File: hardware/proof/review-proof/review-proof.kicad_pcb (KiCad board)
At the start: 4 copper layers, 92 x 60 mm, 26 parts, among them J1 MAINS, J2 5V_IN, J4 LOAD, U1 VO3526, U2 AMS1117-3.3, U3 MCP6001-OT, U4 ATtiny85-20M, Y1 8MHz

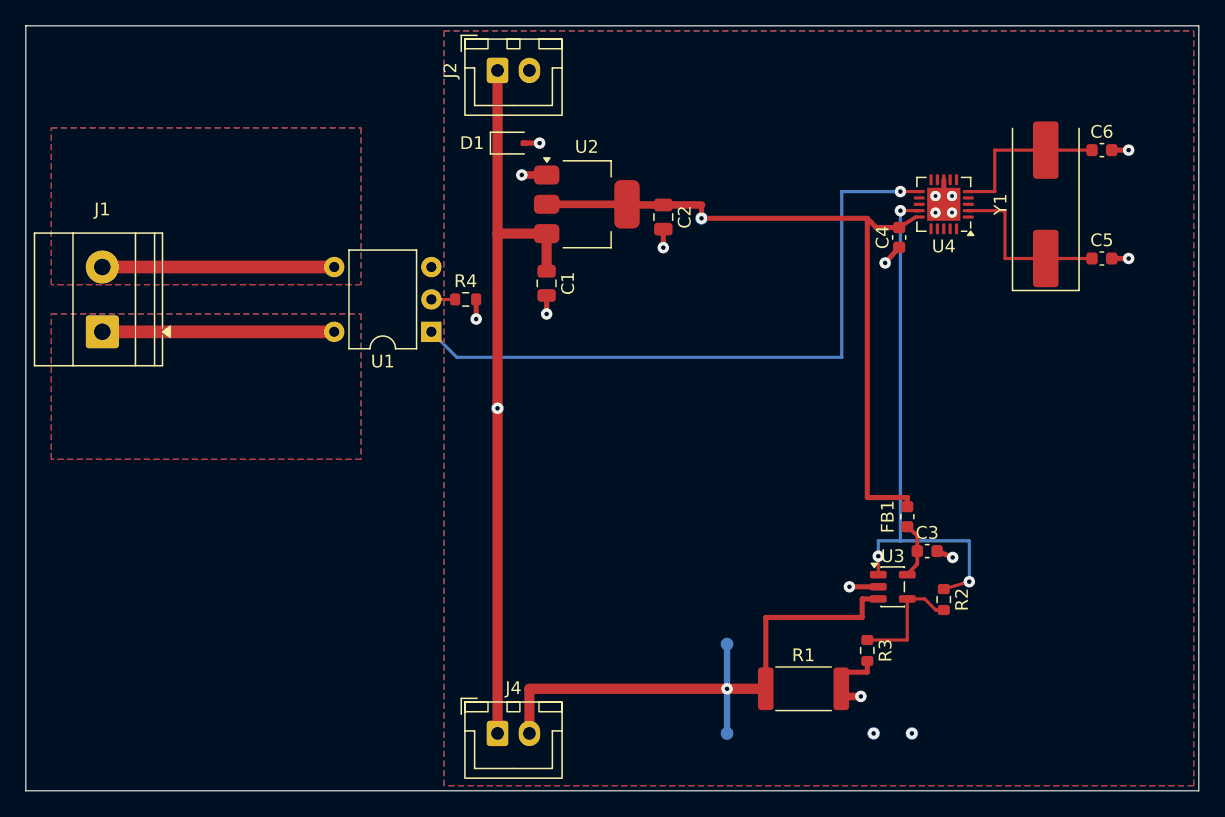
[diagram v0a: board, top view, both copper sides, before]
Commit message: feat(hardware): tidy the review proof design to the workmanship items [SOL-BOARD-LAYOUT-WORKMANSHIP-ITEMS.C3]
Redraw every route of the layout review proof design at 45 degrees, each
straight run at least 1 mm, each track at its class's width and entering
long pads along their axes, branching only at pads, and place R1, R2, R3,
FB1, C3, C4, C5, C6, J4 and the test points beside what they connect to,
so the board passes the pre-order check with every workmanship rule in
force. The tracks, parts and vias are changed through Konnect; the eleven
vias the tidy no longer needs, which Konnect cannot delete, are removed
with KiCad's own scripting API on the closed board. Give the Supply class
a 0.3 mm track width, set the measured rules' figures and the corner and
jog rules, and bring the floorplan, plan and rules table to the board.

Co-Authored-By: Claude Opus 5.5 (1M context) <noreply@anthropic.com>
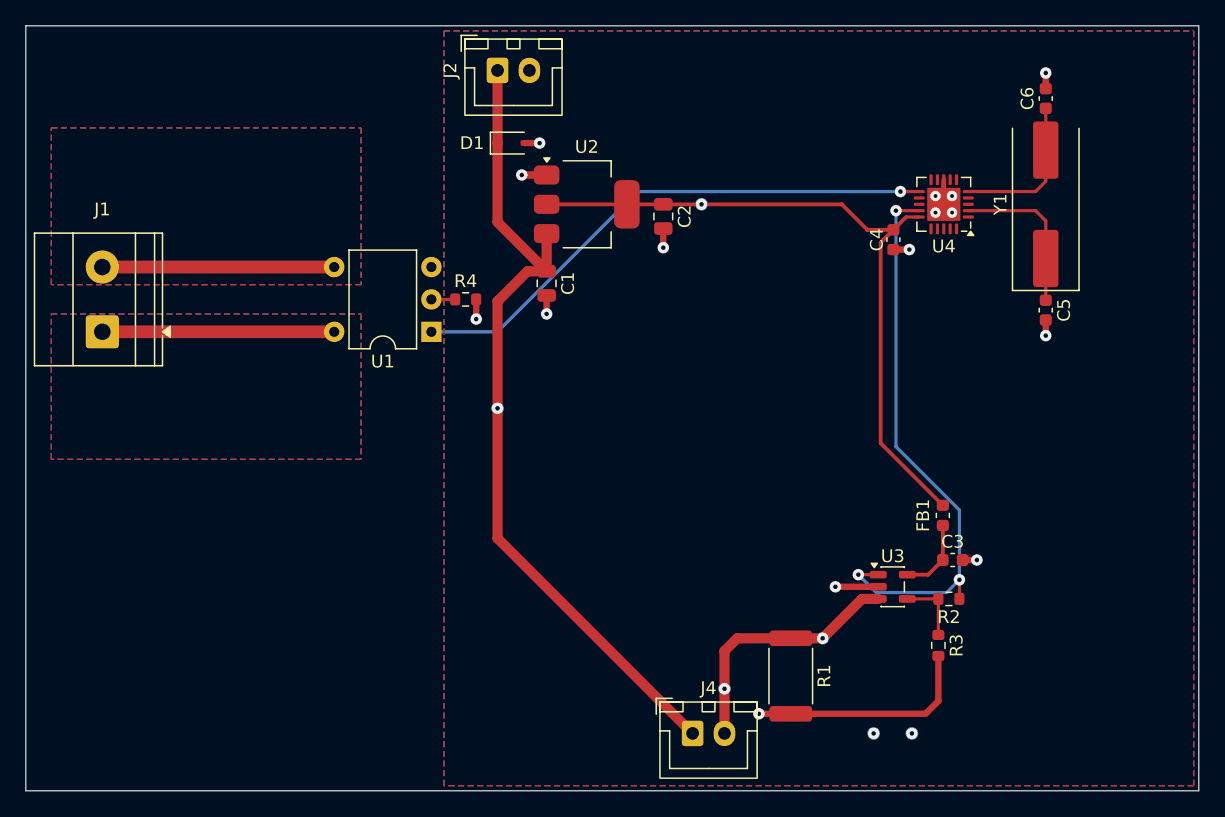
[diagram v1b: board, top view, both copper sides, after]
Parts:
- moved J4 15.3 mm to (52.3, 55.5)
- moved TP4 10.6 mm to (62.5, 48.0)
- moved C5 5.98 mm to (80.0, 22.3), turned to -90 degrees
- moved C6 5.98 mm to (80.0, 5.70), turned to 90 degrees
- moved R3 5.59 mm to (71.6, 48.6)
- moved TP3 3.51 mm to (54.8, 52.0)
- moved FB1 2.79 mm to (71.9, 38.4)
- moved C3 2.12 mm to (72.7, 41.9)
- moved R1 1.41 mm to (60.0, 51.0), turned to -90 degrees
- moved TP2 1.10 mm to (53.0, 14.0)
- moved C4 0.48 mm to (68.0, 16.8)
- moved R2 0.40 mm to (72.4, 45.0), turned to 180 degrees
- moved C2 0.05 mm to (50.0, 14.9)
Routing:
- net /LOAD_RTN: track 44.9 -> 20.2 mm, vias 1 -> 2
- net /GND: track 20.7 -> 35.8 mm
- net /LED_DRV: track 52.1 -> 42.8 mm
- net /+5V: track 58.8 -> 65.4 mm
- net /AMP_FB: track 9.59 -> 5.26 mm
- net /AMP_OUT: track 42.4 -> 44.8 mm
- net /+3V3: track 56.3 -> 54.5 mm
- net /+3V3A: track 4.42 -> 5.98 mm
- net /XTAL1: track 13.5 -> 12.6 mm
- net /XTAL2: track 13.0 -> 12.1 mm

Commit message: feat(board-check): hold tracks meeting at a pad to a figure, and turn the review proof's shunt and supply branches square [SOL-BOARD-LAYOUT-WORKMANSHIP-ITEMS.C2, .C3]
KiCad's corner rule does not compare tracks that meet at a pad, so WORK-4
now also measures the angle between them against WORK_PAD_ANGLE_DEG, with
its tests and seeded fault. On the review proof design, turn R1 so its load
pad faces J4 and the sense and gain-resistor returns leave its pads' far
ends, run the 5 V trunk straight through C1's pad with U2's input taken
square from it, branch FB1's supply square from C2's pad, and pull J4's
body back inside the low-voltage region; the vias this leaves unused are
removed with KiCad's own scripting API on the closed board.

Co-Authored-By: Claude Opus 5.5 (1M context) <noreply@anthropic.com>
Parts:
- moved C1 6.18 mm to (36.0, 16.3), turned to 180 degrees
- moved TP4 5.50 mm to (57.0, 48.7)
- moved TP3 3.50 mm to (54.8, 55.5)
- moved C2 2.15 mm to (51.0, 13.1), turned to 90 degrees
- moved J4 2.00 mm to (50.3, 55.5)
- moved R3 1.15 mm to (70.8, 47.8), turned to 180 degrees
- turned R1 to 0 degrees
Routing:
- net /+3V3: track 54.5 -> 62.7 mm
- net /GND: track 35.8 -> 29.9 mm
- net /+5V: track 65.4 -> 61.4 mm
- net /LOAD_RTN: track 20.2 -> 21.1 mm
